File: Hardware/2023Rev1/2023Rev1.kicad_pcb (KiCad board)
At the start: 2 copper layers, 279.4 x 152.4 mm, 106 parts, among them J1 Conn_01x09, J2 Conn_01x09, J3 Conn_01x04, J4 Conn_01x03, J5 Conn_01x02, J6 Conn_02x03_Counter_Clockwise, J7 RJ45_LED_Shielded, Q1 Q_NMOS_GDS, Q2 Q_NMOS_DGS, Q3 Q_NMOS_DGS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

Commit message: put in constraints for pcb size
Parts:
- moved H5 339.5 mm to (36.8, 154.9)
- moved H4 317.4 mm to (32.8, 34.5)
- moved H1 85.4 mm to (302.1, 158.9)
- moved H6 66.1 mm to (306.2, 30.5)
- moved H2 34.1 mm to (333.9, 48.4)
- moved H3 34.1 mm to (333.9, 39.5)
- moved V1 30.5 mm to (289.6, 69.8)
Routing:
- net CURRENT_SENSE: track 272.0 -> 266.8 mm
- net +3.3V: track 298.7 -> 293.4 mm
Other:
- board size 279.4 x 152.4 mm -> 279.4 x 154.9 mm
- board text added: "Connectors align with this edge"

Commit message: correct board dimensions and started redoing traces
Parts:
- Conn1, J1, J2, J3, J4, J5, J7, U2: moved to B.Cu
- moved R42 112.5 mm to (215.6, 58.4), turned to 180 degrees
- moved R40 109.5 mm to (213.1, 54.4), turned to 0 degrees
- moved D20 106.5 mm to (212.1, 48.8), turned to 0 degrees
- moved R43 106.2 mm to (209.3, 59.4), turned to -90 degrees
- moved R41 100.4 mm to (208.5, 53.3)
- moved R37 94.3 mm to (206.8, 53.3)
- moved U8 93.9 mm to (204.5, 57.9), turned to 180 degrees
- moved R34 92.1 mm to (201.9, 53.3), turned to 90 degrees
- moved D19 88.6 mm to (203.7, 48.8), turned to 0 degrees
- moved R39 83.3 mm to (199.6, 57.9), turned to -90 degrees
- moved R35 82.5 mm to (200.2, 53.3)
- moved D13 78.9 mm to (193.9, 105.7), turned to 180 degrees
- moved D18 73.8 mm to (198.4, 48.8), turned to 0 degrees
- moved R31 71.9 mm to (194.1, 58.7), turned to 180 degrees
- moved R12 71.3 mm to (190.1, 105.7), turned to 180 degrees
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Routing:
- net GATE: track 110.5 -> 0.00 mm, vias 3 -> 0
- net Net-(J4-Pad2): track 101.8 -> 0.00 mm
- net GND: track 113.0 -> 14.7 mm, vias 9 -> 0
- net Net-(J3-Pad1): track 87.3 -> 11.0 mm, vias 2 -> 0
- net Logic Switch: track 87.4 -> 11.9 mm, vias 4 -> 1
- net Net-(J3-Pad3): track 75.6 -> 2.39 mm, vias 1 -> 0
- net +3.3V: track 293.4 -> 221.3 mm
- net CURRENT_SENSE: track 266.8 -> 209.2 mm, vias 2 -> 0
- net unconnected-(U1-Pad3.3V_1): track 57.1 -> 0.00 mm
- net Cell1-SENSE: track 58.6 -> 2.47 mm, vias 1 -> 0
- net cell8: track 61.4 -> 12.9 mm
- net +5V: track 248.6 -> 208.0 mm, vias 6 -> 4
- net cell1: track 58.9 -> 19.4 mm
- net Cell2-SENSE: track 52.9 -> 89.7 mm, vias 1 -> 2
- net Cell8-SENSE: track 48.8 -> 81.9 mm, vias 1 -> 2
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- added copper zone on B.Cu, net Net-(Conn1-Pad2)
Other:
- board size 279.4 x 154.9 mm -> 279.4 x 181.4 mm
- board text removed: "Connectors align with this edge"

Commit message: Ran more traces
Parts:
- moved R21 71.1 mm to (124.4, 59.2), turned to 0 degrees
- moved BZ1 71.0 mm to (116.3, 44.8)
- moved D11 71.0 mm to (124.9, 50.3)
- moved Q2 71.0 mm to (127.0, 55.9)
- moved R4 71.0 mm to (124.9, 46.2)
- moved R45 41.5 mm to (208.5, 41.4)
- moved Q4 41.5 mm to (213.1, 41.4)
- moved D13 32.5 mm to (193.9, 73.2)
- moved R12 32.5 mm to (190.1, 73.2)
- moved U1 32.5 mm to (172.7, 84.3)
- moved R10 28.7 mm to (190.5, 137.2)
- moved R6 28.7 mm to (186.7, 138.4)
- moved R13 28.5 mm to (194.3, 137.2)
- moved U2 14.3 mm to (256.3, 18.0), turned to 0 degrees
- moved R44 12.9 mm to (152.4, 43.2), turned to 0 degrees
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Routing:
- net +5V: track 208.0 -> 331.3 mm, vias 4 -> 11
- net Net-(J3-Pad3): track 2.39 -> 121.5 mm
- net cell8: track 12.9 -> 88.3 mm, vias 0 -> 4
- net cell1: track 19.4 -> 92.1 mm, vias 0 -> 4
- net cell2: track 23.8 -> 92.5 mm, vias 0 -> 7
- net Net-(R10-Pad1): track 2.93 -> 64.9 mm
- net Cell1-SENSE: track 2.47 -> 64.0 mm, vias 0 -> 2
- net unconnected-(U1-Pad3.3V_1): track 0.00 -> 59.9 mm, vias 0 -> 2
- net Net-(Q2-Pad2): track 54.4 -> 2.40 mm
- net cell7: track 29.6 -> 80.2 mm, vias 0 -> 6
- net call6: track 25.4 -> 71.7 mm, vias 0 -> 7
- net cell3: track 22.9 -> 67.1 mm, vias 0 -> 4
- net cell4: track 25.7 -> 66.7 mm, vias 0 -> 7
- net cell5: track 14.2 -> 51.0 mm, vias 0 -> 3
- net Cell3-SENSE: track 77.0 -> 44.5 mm
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
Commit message: finished bms for board review
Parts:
- moved R45 39.4 mm to (210.6, 80.8), turned to 180 degrees
- moved Q4 34.9 mm to (210.6, 76.2), turned to -90 degrees
- moved R12 16.9 mm to (205.7, 79.8), turned to 90 degrees
- moved D13 15.7 mm to (205.7, 83.6), turned to 90 degrees
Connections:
- Q4 pad 2: Logic Switch -> LOGIC_SWITCH
- R45 pad 2: Logic Switch -> LOGIC_SWITCH
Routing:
- net +3.3V: track 221.3 -> 365.7 mm, vias 2 -> 7
- net Net-(J3-Pad1): track 11.0 -> 149.3 mm, vias 0 -> 2
- net Net-(Q4-Pad1): track 0.00 -> 104.1 mm, vias 0 -> 3
- net Net-(Q2-Pad2): track 2.40 -> 97.5 mm, vias 0 -> 1
- net GATE: track 0.00 -> 86.4 mm, vias 0 -> 2
- net Net-(J4-Pad2): track 0.00 -> 85.2 mm, vias 0 -> 2
- net Net-(Q3-Pad2): track 2.33 -> 84.8 mm, vias 0 -> 2
- net CURRENT_SENSE: track 209.2 -> 253.2 mm, vias 0 -> 2
- net LOGIC_SWITCH: track 0.00 -> 33.1 mm
- net ERR_LED: track 3.56 -> 17.4 mm
- net Logic Switch: track 6.30 -> 0.00 mm
- net +5V: track 331.3 -> 332.4 mm
- net cell3: vias 4 -> 6
- net Net-(F1-Pad2): vias 0 -> 66
- net Net-(C2-Pad1): vias 0 -> 59

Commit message: Fixes from layout review
Fixed rx diff pair
Via stitched some power plains
Big via spacing from edge
Changed teensy 5v input to vin
Fixed ground plane clearance
Silk screen labels for LEDs
Fixed 90s
Fixed thermal relief on plane
Fixed plane spacing next to one another
1500 mil planes
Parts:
- Conn1: footprint MRDT_Connectors:Square_Anderson_2_V_Side_By_Side_PV -> MRDT_Connectors:Anderson_2_Horizontal_Side_by_Side
- moved D9 193.7 mm to (69.6, 47.2), turned to 0 degrees
- moved R2 186.5 mm to (73.7, 47.2), turned to 0 degrees
- moved Conn1 146.8 mm to (278.5, 32.4), turned to -90 degrees
- moved D13 140.2 mm to (69.6, 50.3), turned to 0 degrees
- moved R12 135.3 mm to (73.7, 50.3), turned to 0 degrees
- moved D12 112.6 mm to (69.6, 53.3), turned to 0 degrees
- moved R8 69.1 mm to (71.1, 132.1)
- moved D11 55.7 mm to (69.6, 43.7), turned to 0 degrees
- moved R4 51.3 mm to (73.7, 43.7), turned to 0 degrees
- moved C8 44.2 mm to (261.6, 170.4), turned to -90 degrees
- moved Q1 27.3 mm to (226.5, 134.1)
- moved U4 26.6 mm to (267.6, 173.3)
- moved F1 25.2 mm to (265.2, 132.3)
- moved V1 15.5 mm to (308.6, 106.9)
- moved V2 15.5 mm to (308.6, 151.3)
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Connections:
- U1 pad 5V: +5V -> unconnected-(U1-Pad5V)
- U1 pad VIN: unconnected-(U1-PadVIN) -> +5V
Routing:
- net ERR_LED: track 17.4 -> 144.8 mm, vias 0 -> 2
- net +3.3V: track 365.7 -> 484.1 mm, vias 7 -> 9
- net Net-(Conn1-Pad2): track 0.00 -> 107.6 mm
- net Net-(D12-Pad2): track 3.50 -> 78.1 mm
- net +5V: track 332.4 -> 396.9 mm
- net Net-(C8-Pad1): track 15.7 -> 0.00 mm
- net GND: track 14.7 -> 0.00 mm, vias 0 -> 21
- net CURRENT_SENSE: track 253.2 -> 265.9 mm, vias 2 -> 4
- net Net-(J5-Pad1): track 23.2 -> 13.3 mm
- net Net-(Q3-Pad2): track 84.8 -> 94.7 mm
- net Net-(Q1-Pad1): track 6.89 -> 0.00 mm
- net Net-(R10-Pad1): track 64.9 -> 58.3 mm
- net unconnected-(U1-Pad3.3V_1): track 59.9 -> 53.9 mm
- net Net-(Q2-Pad2): track 97.5 -> 93.9 mm, vias 1 -> 2
- net Net-(J3-Pad1): track 149.3 -> 147.1 mm, vias 2 -> 3
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- removed copper zone on B.Cu, net Net-(F1-Pad2)
- removed copper zone on F.Cu, net Net-(F1-Pad2)
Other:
- board text added: "+3.3V"
- board text added: "+5V"
- board text added: "ERR"
- board text added: "PACK_OUT"

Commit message: added LCD pinout, more plane stitching
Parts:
- added J8: Conn_01x03, MRDT_Connectors:MOLEX_SL_03_Vertical, F.Cu at (139.7, 17.8)
- moved R32 11.0 mm to (250.7, 126.2), turned to 0 degrees
- moved R38 7.74 mm to (214.6, 131.3), turned to 180 degrees
- moved R36 6.63 mm to (218.7, 132.3)
- moved U10 4.33 mm to (250.7, 131.1)
- moved R21 3.84 mm to (128.3, 59.4)
- moved Q2 0.90 mm to (126.5, 56.6), turned to 180 degrees
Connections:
- U1 pad 1: unconnected-(U1-Pad1) -> LCD_TX
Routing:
- net Net-(F1-Pad2): track 0.00 -> 111.2 mm
- net LCD_TX: track 0.00 -> 94.0 mm, vias 0 -> 2
- net +3.3V: track 484.1 -> 533.7 mm, vias 9 -> 10
- net Net-(Q1-Pad1): track 0.00 -> 23.2 mm
- net Net-(J3-Pad3): track 121.5 -> 116.6 mm
- net Net-(Q2-Pad2): track 93.9 -> 92.1 mm
- net Net-(J3-Pad1): track 147.1 -> 148.8 mm
- net Net-(BZ1-Pad2): track 10.3 -> 11.7 mm
- net PACK_OUT: vias 2 -> 66
- net Net-(Conn1-Pad2): vias 0 -> 29
- net Net-(C8-Pad1): vias 0 -> 6
- net (no net): vias 64 -> 7

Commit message: BEMIS FINISHED
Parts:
- moved H2 151.4 mm to (263.5, 194.5)
- moved H3 114.5 mm to (254.1, 70.0)
- moved C2 50.8 mm to (241.6, 42.4), turned to 90 degrees
- moved C5 42.5 mm to (241.6, 50.0), turned to 90 degrees
- moved C3 41.1 mm to (232.4, 66.0)
- moved C4 40.6 mm to (241.3, 65.9)
- moved U6 39.4 mm to (244.2, 55.9)
- moved C6 32.0 mm to (223.8, 45.0)
- moved U2 26.7 mm to (229.9, 18.0)
- moved C7 22.9 mm to (223.8, 61.7)
- moved U9 19.5 mm to (234.9, 48.7), turned to 90 degrees
- moved F1 9.65 mm to (255.5, 132.5)
- moved U10 4.07 mm to (246.6, 131.2)
- moved R32 3.83 mm to (246.9, 126.6)
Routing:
- net +5V: track 396.6 -> 346.3 mm, vias 11 -> 9
- net Net-(C2-Pad1): track 0.00 -> 50.2 mm, vias 59 -> 0
- net Net-(Q4-Pad1): track 104.4 -> 74.9 mm, vias 3 -> 4
- net +3.3V: track 533.7 -> 556.5 mm, vias 10 -> 9
- net Net-(F1-Pad2): track 111.2 -> 118.4 mm
- net Net-(J3-Pad1): track 148.8 -> 144.3 mm
- net Net-(Q1-Pad1): track 23.2 -> 19.2 mm
- removed copper zone on B.Cu, net Net-(C2-Pad1)
- removed copper zone on F.Cu, net Net-(C2-Pad1)

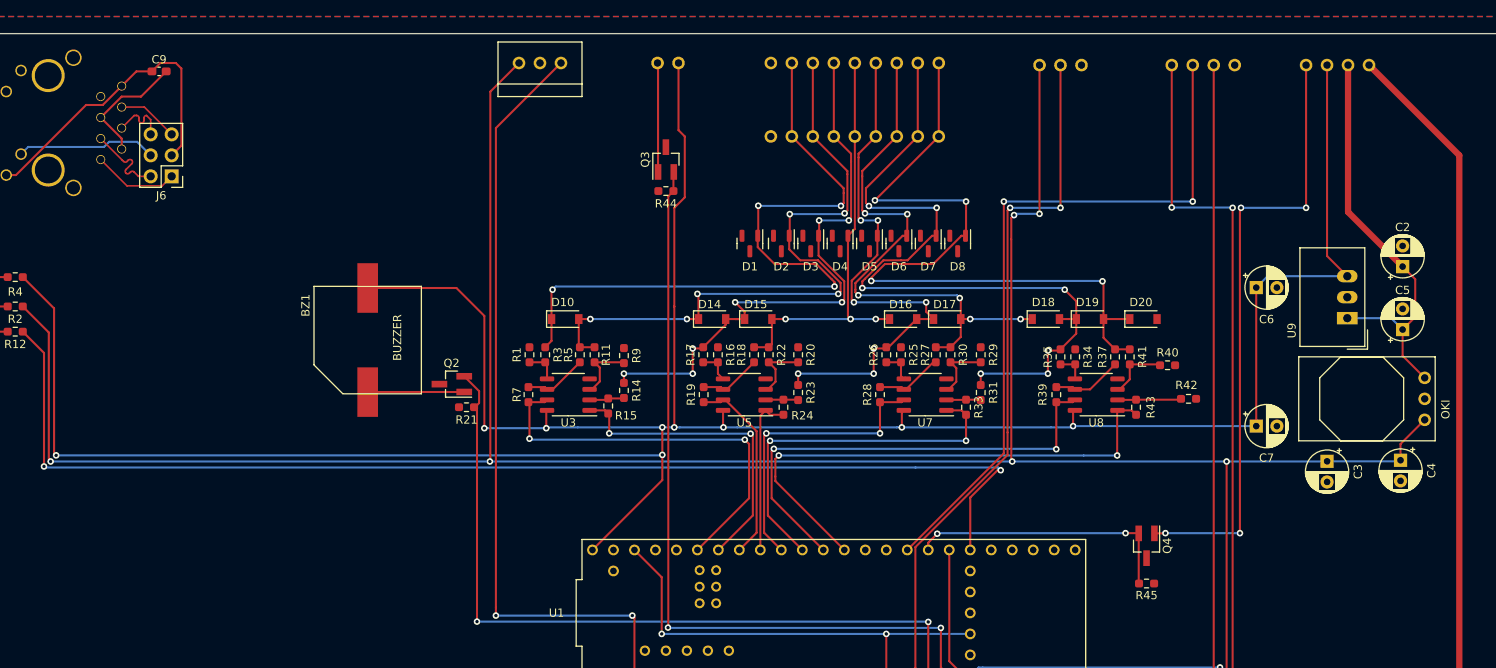
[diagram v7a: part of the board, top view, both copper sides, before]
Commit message: replaced tht caps with smd
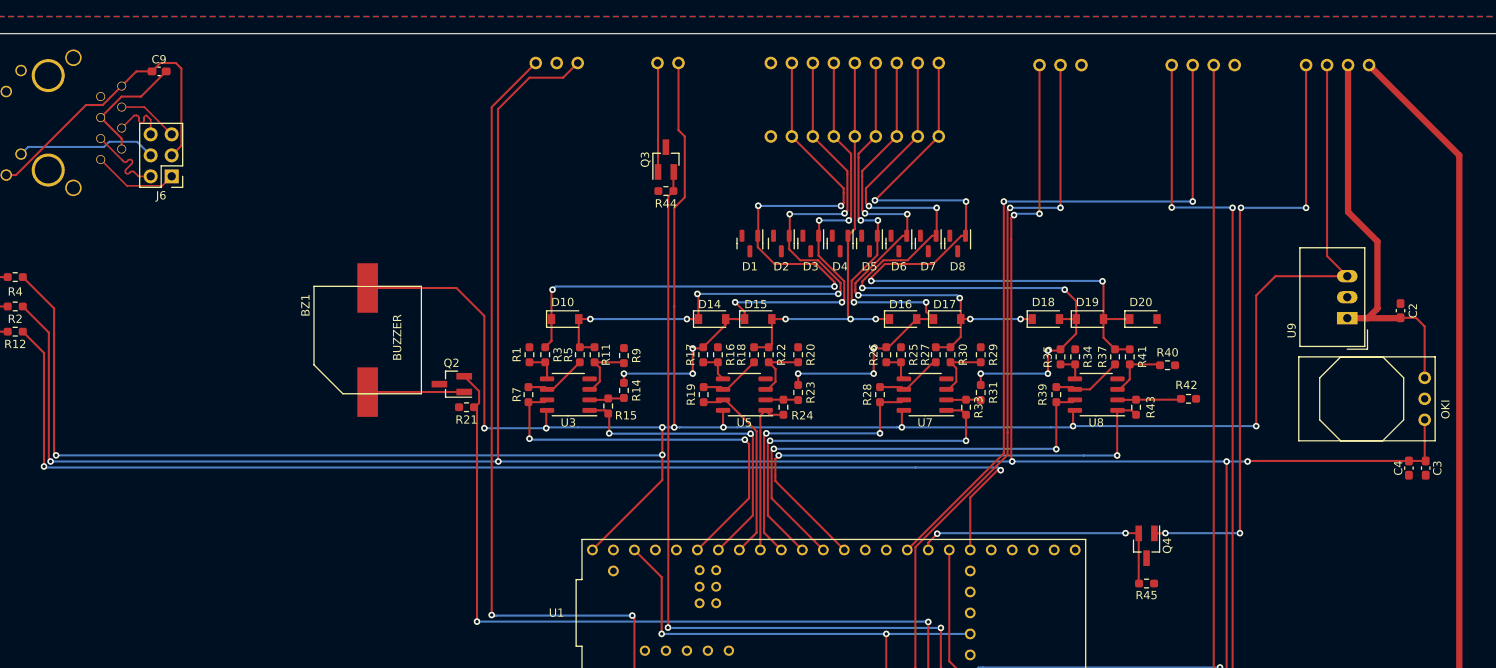
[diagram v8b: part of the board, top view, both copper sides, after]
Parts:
- removed C5: 22uF, Capacitor_THT:CP_Radial_D5.0mm_P2.50mm
- removed C6: 1uF, Capacitor_THT:CP_Radial_D5.0mm_P2.50mm
- removed C7: 10uF, Capacitor_THT:CP_Radial_D5.0mm_P2.50mm
- C2, C3, C4: footprint Capacitor_THT:CP_Radial_D5.0mm_P2.50mm -> Capacitor_SMD:C_0603_1608Metric_Pad1.08x0.95mm_HandSolder
- J8: moved to B.Cu
- moved C3 12.0 mm to (244.3, 66.8)
- moved C2 5.34 mm to (241.3, 47.8)
- moved J8 3.05 mm to (136.7, 17.8), turned to 0 degrees
- moved C4 1.39 mm to (242.3, 66.8)
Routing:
- net +3.3V: track 556.5 -> 563.7 mm, vias 9 -> 10
- net Net-(C2-Pad1): track 50.2 -> 48.6 mm
- net +5V: track 346.3 -> 345.4 mm, vias 9 -> 10
- net LCD_TX: track 94.0 -> 93.5 mm
